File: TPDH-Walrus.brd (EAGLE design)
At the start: 16 x 49.4 mm, 34 parts, among them Q2 DMG3404, U1 MS5803-14BA, U2 SN65HVD33RHL

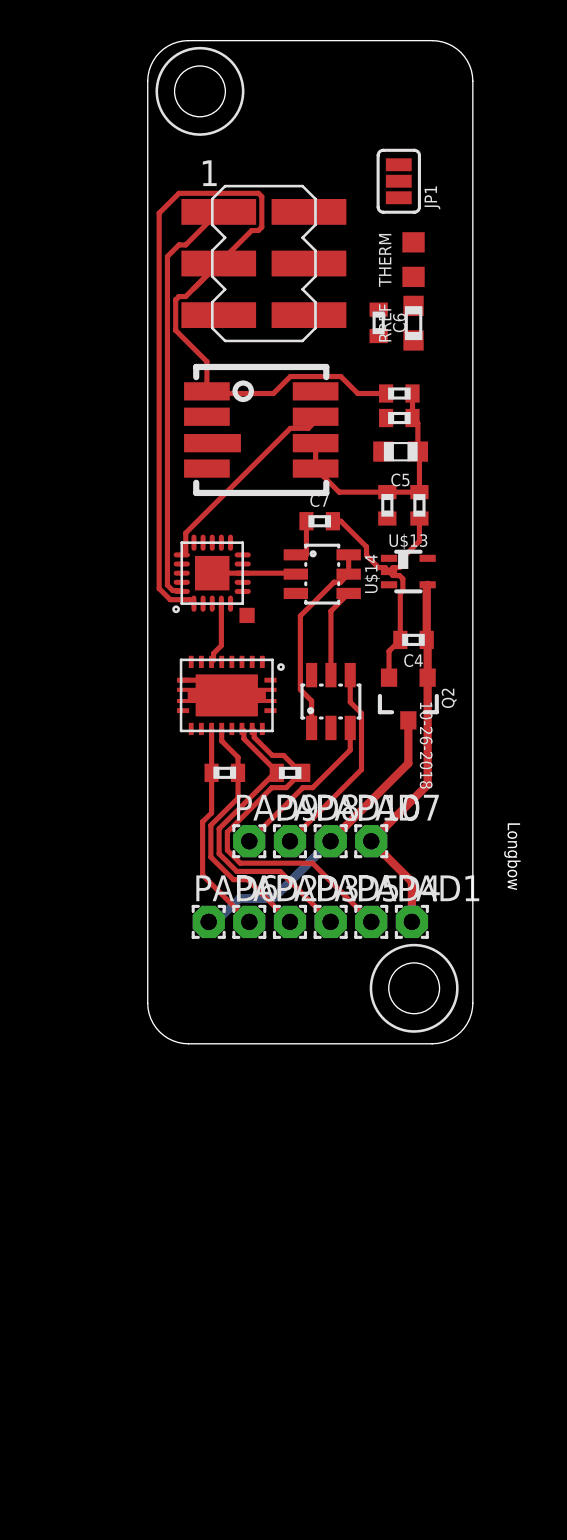
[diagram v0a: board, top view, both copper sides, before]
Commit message: PTH ISP, more routing
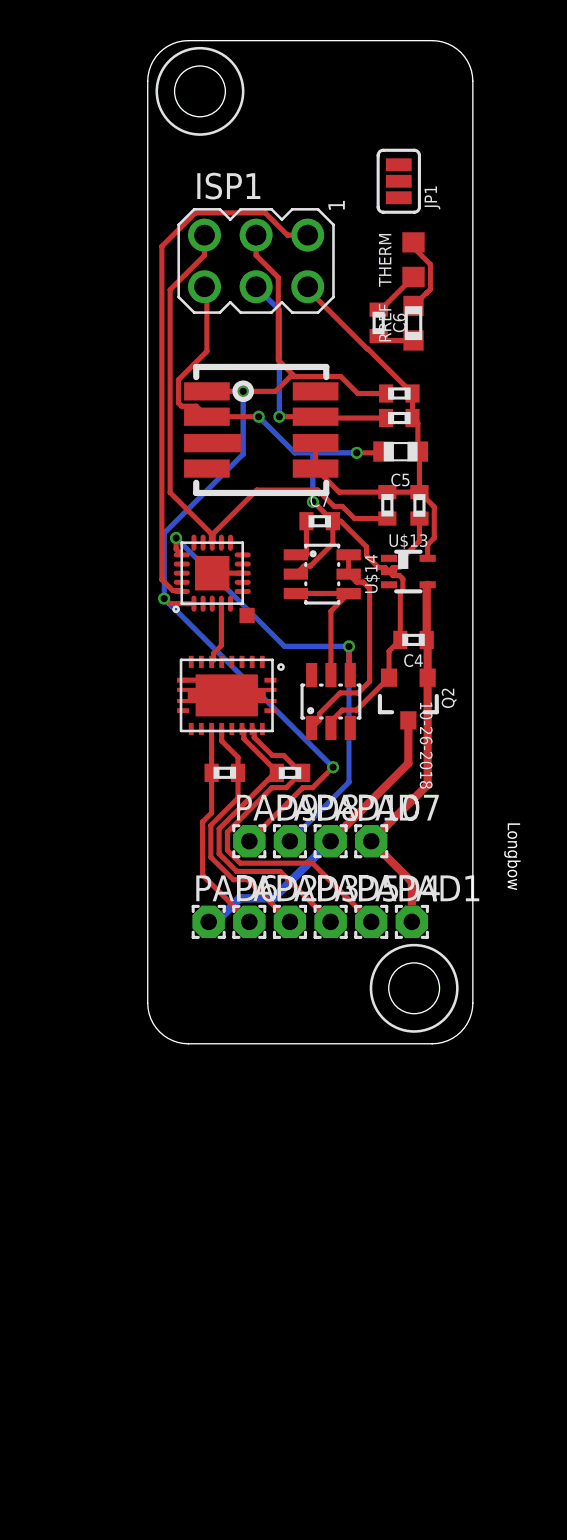
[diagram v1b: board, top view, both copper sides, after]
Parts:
- ISP1: value AVRISP -> AVRISP-6; device bschulz:2X3_SMD -> bschulz:AVRISP
- moved ISP1 0.40 mm to (5.33, 38.5)
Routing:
- net GND: track 20.0 -> 48.1 mm, vias 0 -> 3
- net /RESET: track 0.00 -> 27.2 mm
- net SDA: track 19.9 -> 36.3 mm, vias 0 -> 3
- net 3V3: track 16.2 -> 29.9 mm
- net SCL: track 57.6 -> 48.5 mm, vias 0 -> 3
- net MISO: track 20.4 -> 25.9 mm
- net VTHERM-: track 0.00 -> 3.83 mm
- net VREF: track 9.92 -> 13.3 mm

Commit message: multiple schematic and layout updates * status indicator * LDO reset * move thermistor by power supply and voltage reference * rip up traces and reorganize
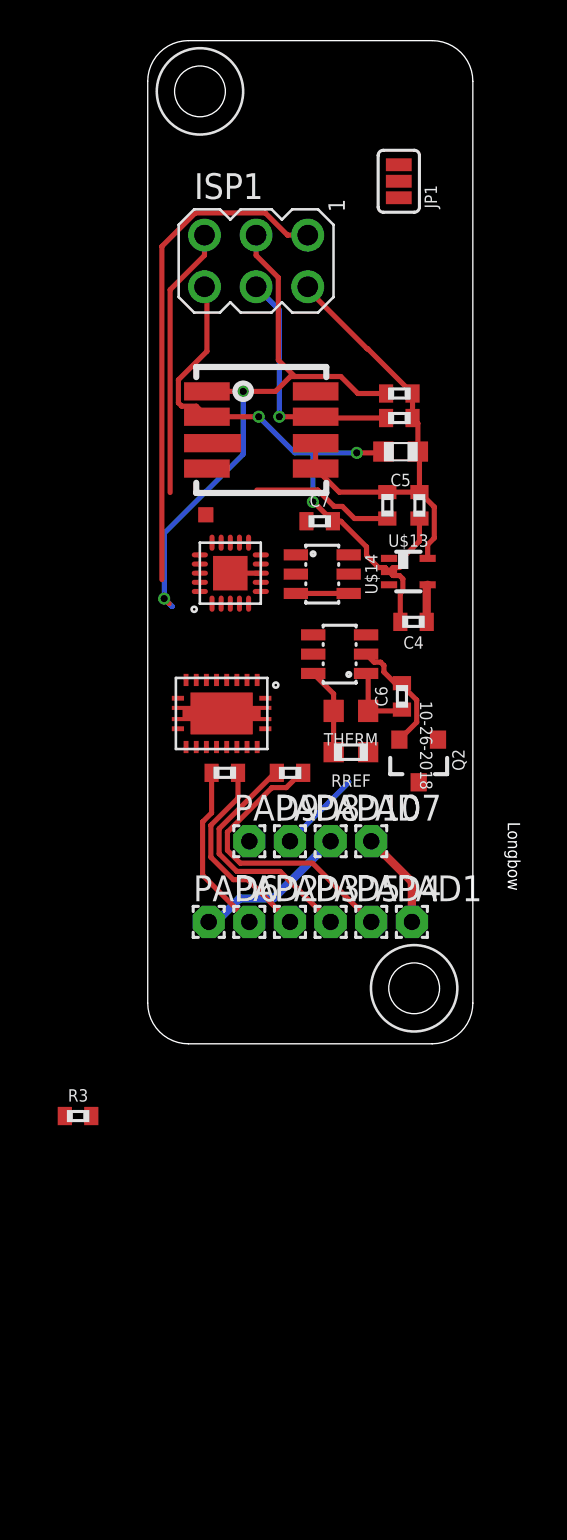
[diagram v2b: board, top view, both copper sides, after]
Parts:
- added R3: 10k, bschulz_passives:R0402
- moved THERM 22.4 mm to (10.0, 16.4), turned to 180 degrees
- moved RREF 21.3 mm to (10.0, 14.4), turned to 180 degrees
- moved C6 18.4 mm to (12.5, 17.1), turned to 90 degrees
- moved U$12 5.35 mm to (2.86, 26.0)
- moved Q2 3.09 mm to (13.3, 14.0)
- moved U$2 2.37 mm to (9.45, 19.2), turned to 90 degrees
- moved U2 0.92 mm to (3.64, 16.3)
- moved U$4 0.89 mm to (4.06, 23.2)
- moved C4 0.89 mm to (13.1, 20.8)
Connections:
- new net PG: R3.1, U$13.1, U$4.2
- new net SN_DE: U$4.12, U2.6
- new net SN_RE: U$4.11, U2.4
- new net VCC: R3.2
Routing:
- net SDA: track 36.3 -> 16.5 mm, vias 3 -> 1
- net SCL: track 48.5 -> 30.5 mm, vias 3 -> 2
- net VIN+: track 18.6 -> 6.64 mm
- net VREF: track 13.3 -> 3.57 mm
- net GND: track 48.1 -> 39.2 mm
- net VIN-: track 15.2 -> 7.64 mm
- net /RESET: track 27.2 -> 20.4 mm
- net 3V3: track 29.9 -> 25.5 mm
- net RX+: track 17.9 -> 14.3 mm
- net TX: track 3.07 -> 0.00 mm
- net RX-: track 15.1 -> 12.2 mm
- net TX-: track 12.4 -> 9.91 mm
- net N$11: track 2.18 -> 0.00 mm
- net TX+: track 10.6 -> 8.47 mm
- net MISO: track 25.9 -> 24.7 mm

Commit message: ATTiny1634 on schematic
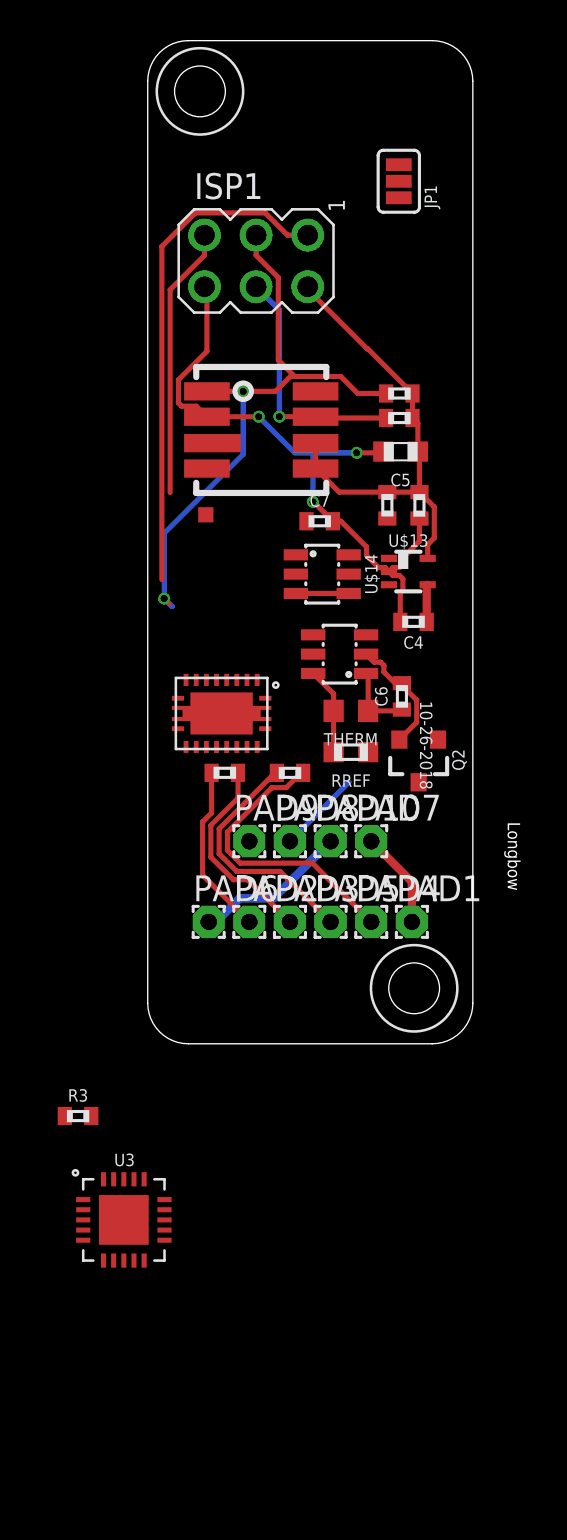
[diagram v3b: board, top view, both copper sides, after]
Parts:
- removed U$4: ATTINY441/841VQFN, bschulz:VQFN-20
- added U3: (no value), bschulz:QFN20
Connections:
- new net N$10: U3.11
- new net N$12: U3.10
- new net N$13: U3.3
- new net N$14: U3.2
- new net N$15: U3.1
- new net N$2: U3.7
- new net N$3: U3.6
- new net N$5: U3.16
- new net N$6: U3.15
- new net N$7: U3.5
- new net N$8: U3.13
- new net N$9: U3.4
- net /RESET: now also U3.12; no longer U$4.13
- net 3V3: now also U3.9; no longer U$4.9
- net GND: now also U3.8, U3.EP; no longer U$4.8, U$4.EP
- net MISO: now also U3.17; no longer U$4.20
- net PG: no longer U$4.2
- net RX: now also U3.20; no longer U$4.3
- net SCL: now also U3.14; no longer U$4.1
- net SDA: now also U3.18; no longer U$4.16
- net SN_DE: no longer U$4.12
- net SN_RE: no longer U$4.11
- net TEST_PIN: no longer U$4.5
- net TX: now also U3.19; no longer U$4.4
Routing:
- net /RESET: track 20.4 -> 13.4 mm
- net GND: track 39.2 -> 37.7 mm

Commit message: Level shifter on schematic
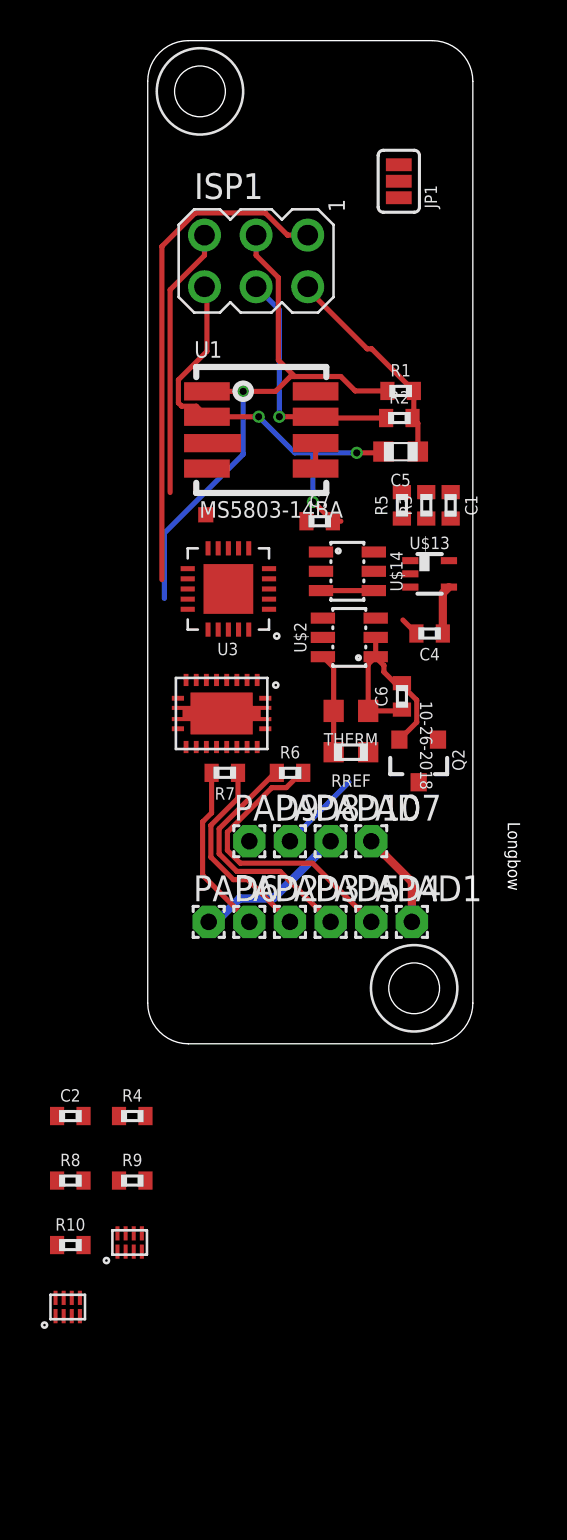
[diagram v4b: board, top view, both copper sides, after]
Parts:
- added C2: 0.1uF, bschulz_passives:C0402
- added R10, R4, R8, R9: 10k, bschulz_passives:R0402
- added U$3, U$6: TXS0102DQM, bschulz:DQM_R-PX2SON-N8
- moved R3 34.6 mm to (13.7, 26.5), turned to 90 degrees
- moved U3 31.4 mm to (3.94, 22.4), turned to 180 degrees
- moved C1 1.54 mm to (14.9, 26.5)
- moved U$14 1.24 mm to (9.83, 23.3)
- moved U$13 1.05 mm to (13.9, 23.1)
- moved C4 0.98 mm to (13.9, 20.2)
- moved U$2 0.95 mm to (9.92, 20.0)
- moved R5 0.72 mm to (12.5, 26.5)
- moved R1 0.14 mm to (12.4, 32.1)
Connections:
- removed net VCC: R3.2
- new net RX_HV: U$6.7
- new net SCL_HV: R9.1, U$3.7
- new net SDA_HV: R10.1, U$3.6
- new net TX_HV: U$6.6
- new net UART_EN: U$6.5
- net 3V3: now also R3.2, R4.2, R8.2, U$3.1, U$3.5, U$6.1
- net GND: now also C2.2, U$3.4, U$6.4
- net RX: now also U$6.2
- net SCL: now also R4.1, U$3.2
- net SDA: now also R8.1, U$3.3
- net TX: now also U$6.3
- net VIN+: now also C2.1, R10.2, R9.2, U$3.8, U$6.8
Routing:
- net 3V3: track 25.5 -> 14.4 mm
- net GND: track 37.7 -> 29.0 mm
- net SCL: track 30.5 -> 29.0 mm, vias 2 -> 1
- net VREF: track 3.57 -> 4.51 mm
- net VTHERM-: track 4.29 -> 4.92 mm
- net VIN+: track 6.64 -> 7.21 mm

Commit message: Connected level shifter, added passives
Added schematic connections for level shifter, also added decoupling capacitors and relabeled IC values
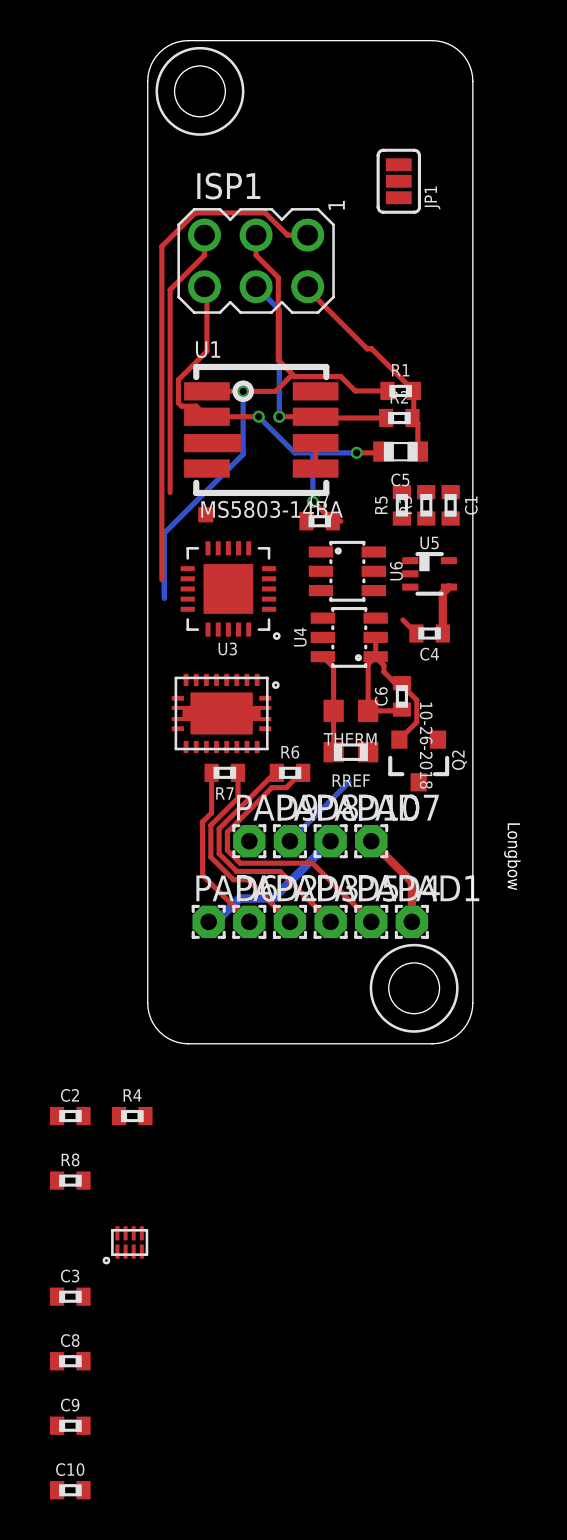
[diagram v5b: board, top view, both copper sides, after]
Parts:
- removed R10, R9: 10k, bschulz_passives:R0402
- removed U$6: TXS0102DQM, bschulz:DQM_R-PX2SON-N8
- added C10, C3, C8, C9: 0.1uF, bschulz_passives:C0402
- R1, R2: value 3k -> 4.7k
- renumbered U$13 to U5, U$14 to U6, U$2 to U4, U$3 to U7
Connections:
- removed net RX_HV: U$6.7
- removed net TX_HV: U$6.6
- removed net UART_EN: U$6.5
- new net REF_EN: U6.3
- net 3V3: now also C10.1, C3.1, C8.1, C9.1; no longer R4.2, R8.2, U$6.1, U6.3
- net GND: now also C10.2, C3.2, C8.2, C9.2; no longer U$6.4
- net RX: no longer U$6.2
- net SCL: no longer PAD9.1, R4.1
- net SCL_HV: now also PAD9.1, R4.1; no longer R9.1
- net SDA: no longer PAD8.1, R8.1
- net SDA_HV: now also PAD8.1, R8.1; no longer R10.1
- net TX: no longer U$6.3
- net VIN+: now also R4.2, R8.2; no longer R10.2, R9.2, U$6.8
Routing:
- net SDA: track 16.5 -> 12.4 mm
- net SDA_HV: track 0.00 -> 4.11 mm
- net 3V3: track 14.4 -> 11.8 mm

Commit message: all components approx placed
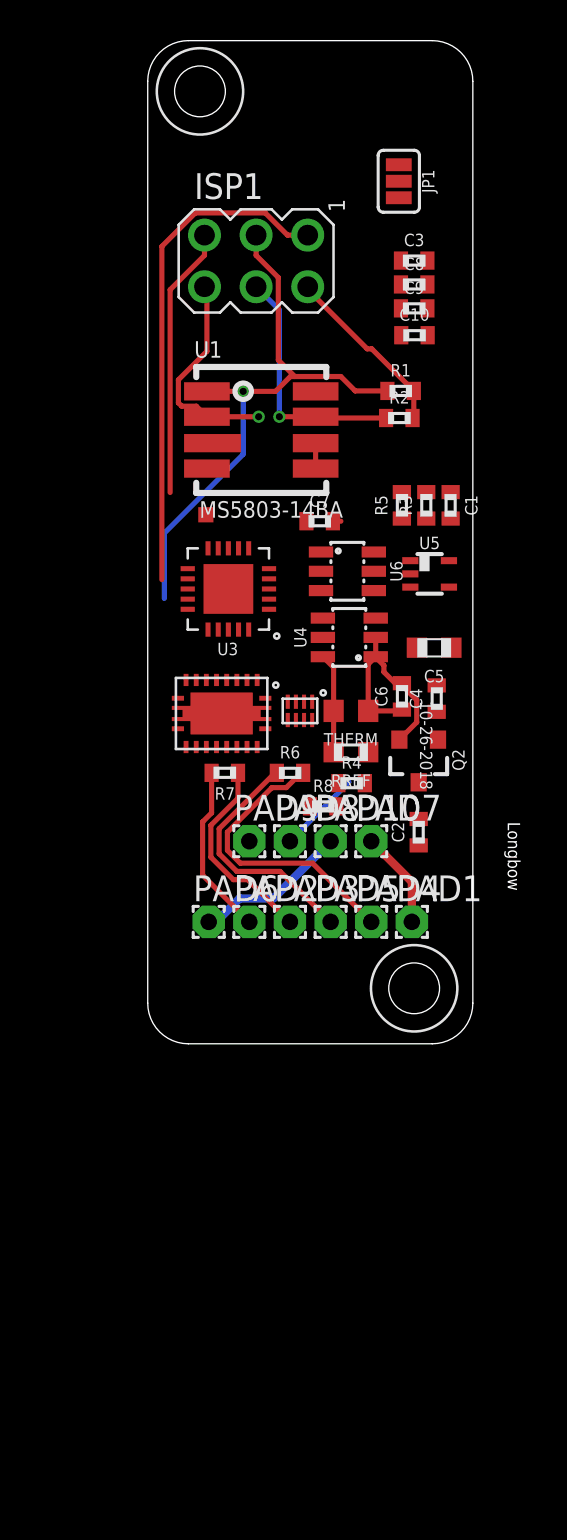
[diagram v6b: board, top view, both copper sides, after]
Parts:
- moved C10 59.3 mm to (13.1, 34.9)
- moved C9 57.5 mm to (13.1, 36.2)
- moved C8 55.6 mm to (13.1, 37.4)
- moved C3 53.7 mm to (13.1, 38.5)
- moved U7 27.5 mm to (7.49, 16.4), turned to 180 degrees
- moved R8 22.2 mm to (8.64, 11.7)
- moved C2 22.1 mm to (13.3, 10.4), turned to 90 degrees
- moved R4 19.6 mm to (10.0, 12.8)
- moved C5 9.79 mm to (14.1, 19.5)
- moved C4 3.22 mm to (14.2, 17.0), turned to 90 degrees
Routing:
- net GND: track 29.0 -> 17.5 mm, vias 3 -> 1
- net VIN+: track 7.21 -> 4.80 mm
- net 3V3: track 11.8 -> 10.0 mm

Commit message: Routed
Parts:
- added H3: (no value), bschulz:2_56
- moved H1 14.4 mm to (13.3, 37.2)
- moved JP1 12.6 mm to (2.12, 35.1), turned to 90 degrees
- moved C3 9.41 mm to (14.5, 29.2)
- moved C8 9.33 mm to (14.5, 28.1)
- moved C9 9.25 mm to (14.5, 27.1)
- moved C10 9.02 mm to (14.5, 26.0)
- moved C2 6.79 mm to (14.2, 17.1)
- moved R5 4.30 mm to (14.5, 30.3), turned to 180 degrees
- moved ISP1 2.83 mm to (7.16, 36.4)
- moved C4 2.51 mm to (13.6, 19.4), turned to 180 degrees
- moved R3 2.46 mm to (11.4, 27.3), turned to 0 degrees
- moved R2 1.77 mm to (11.3, 29.4), turned to 270 degrees
- moved C1 1.71 mm to (14.5, 24.8), turned to 180 degrees
- moved C5 1.61 mm to (13.6, 21.0)
- moved R8 1.40 mm to (10.0, 11.7)
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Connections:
- removed net N$12: U3.10
- removed net N$13: U3.3
- removed net N$3: U3.6
- removed net N$5: U3.16
- removed net N$6: U3.15
- net PG: now also U3.6
- net REF_EN: now also U3.3
- net SN_DE: now also U3.15
- net SN_RE: now also U3.16
- net TEST_PIN: now also U3.10
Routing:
- net 3V3: track 10.0 -> 77.7 mm, vias 0 -> 10
- net GND: track 17.5 -> 76.8 mm, vias 1 -> 4
- net SDA: track 12.4 -> 41.1 mm, vias 1 -> 4
- net SCL: track 29.0 -> 53.1 mm, vias 1 -> 3
- net VIN+: track 4.80 -> 25.7 mm
- net /RESET: track 13.4 -> 34.1 mm
- net PG: track 0.00 -> 11.3 mm
- net TX: track 0.00 -> 9.11 mm, vias 0 -> 2
- net SCL_HV: track 0.00 -> 8.94 mm
- net VREF: track 4.51 -> 12.8 mm, vias 0 -> 2
- net N$1: track 0.00 -> 8.04 mm
- net VIN-: track 7.64 -> 15.2 mm, vias 0 -> 1
- net RX: track 0.00 -> 7.08 mm
- net SDA_HV: track 4.11 -> 9.18 mm, vias 0 -> 1
- net SN_DE: track 0.00 -> 4.17 mm
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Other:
- board size 16 x 49.4 mm -> 16 x 39.9 mm
